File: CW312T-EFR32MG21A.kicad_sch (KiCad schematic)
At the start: 18 parts, among them J1 1x3 straight header pins, P1 PCIEx4 EDGE CONNECTOR, U1 EFR32MG21A020F1024IM32-BR

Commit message: first draft - ready for review
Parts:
- added PCB1: CE Symbol, Silkscrren_Symbols:CE-Logo_8.5x6mm_SilkScreen, symbol Silkscreen_Symbols:CE_Free
- added PCB2: Pb_Free Symbol, Silkscrren_Symbols:Pb_Free_8.0x8.0mm_SilkScreen, symbol Silkscreen_Symbols:Pb_Free
- added PCB3: UKCA symbol, Silkscrren_Symbols:UKCA-Logo_8x8mm_SilkScreen, symbol Silkscreen_Symbols:UKCA
- added PCB4: WEEE SYMBOL, Silkscrren_Symbols:WEEE-Logo_5.6x8mm_SilkScreen, symbol Silkscreen_Symbols:WEEE
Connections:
- net GND: now also U1.33 (VSS); no longer U1.0 (VSS)

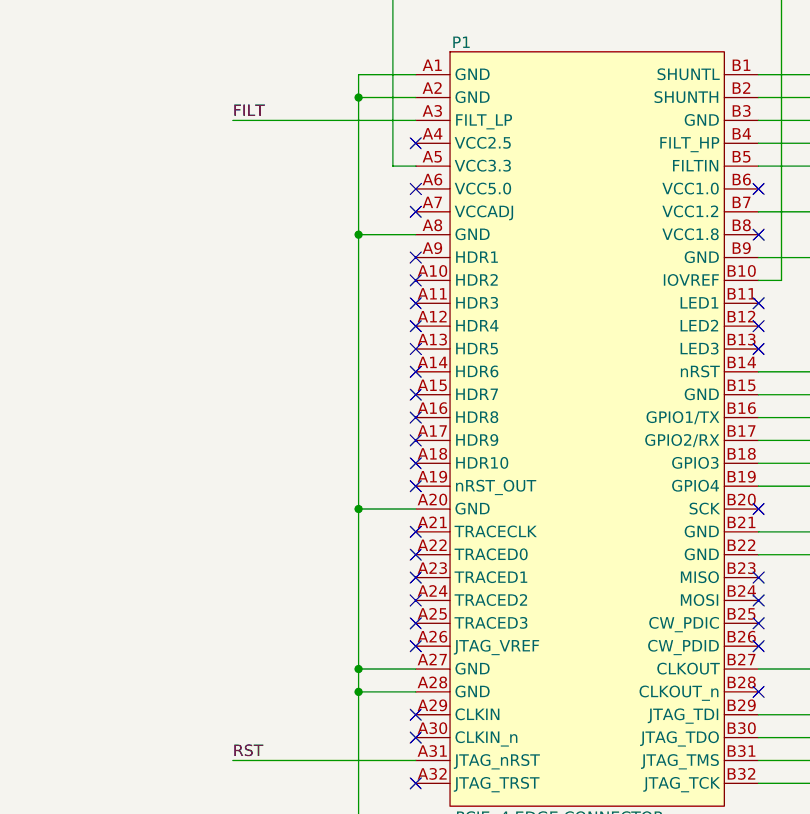
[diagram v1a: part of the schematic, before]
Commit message: updated schematic to fix power, updated pcb and production files - ready for review
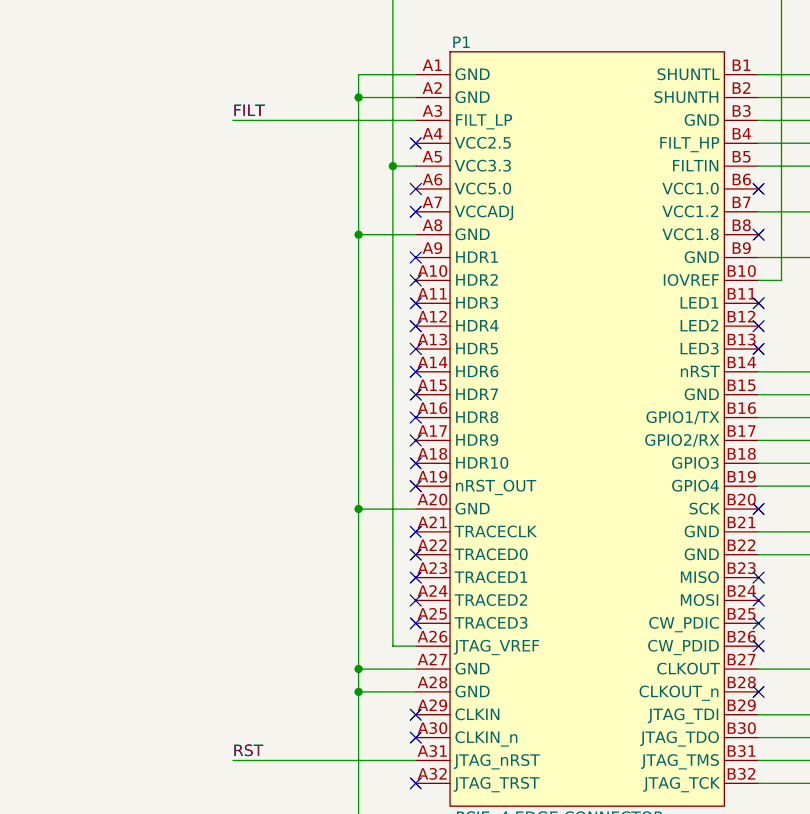
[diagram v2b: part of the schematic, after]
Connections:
- net +3V3: now also P1.A26 (JTAG_VREF)
- no-connect marks 47 -> 46
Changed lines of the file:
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@@
+	)
+	(junction
+		(at 39.37 62.23)
+		(diameter 0)
+		(color 0 0 0 0)
 	)
 	(junction
@@
 	)
 	(no_connect
-		(at 41.91 115.57)
-	)
-	(no_connect
 		(at 41.91 107.95)
 	)
@@
 	(wire
 		(pts
+			(xy 39.37 62.23) (xy 39.37 115.57)
+		)
+		(stroke
+			(width 0)
+			(type default)
+		)
+	)
+	(wire
+		(pts
 			(xy 35.56 120.65) (xy 41.91 120.65)
 		)
@@
 		)
 		(stroke
+			(width 0)
+			(type default)
+		)
+	)
+	(wire
+		(pts
+			(xy 41.91 115.57) (xy 39.37 115.57)
+		)
+		(stroke

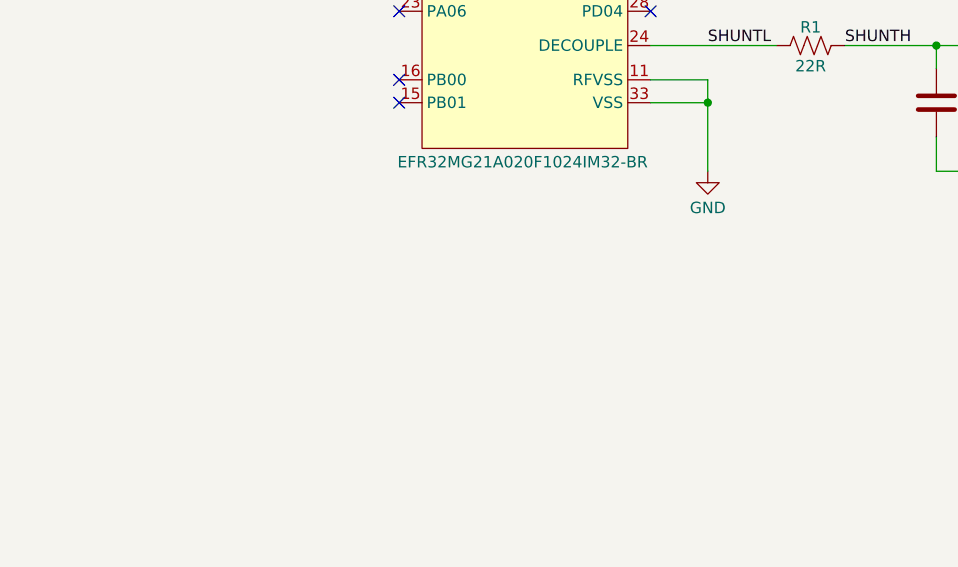
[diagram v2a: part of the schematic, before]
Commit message: added comment about footprint
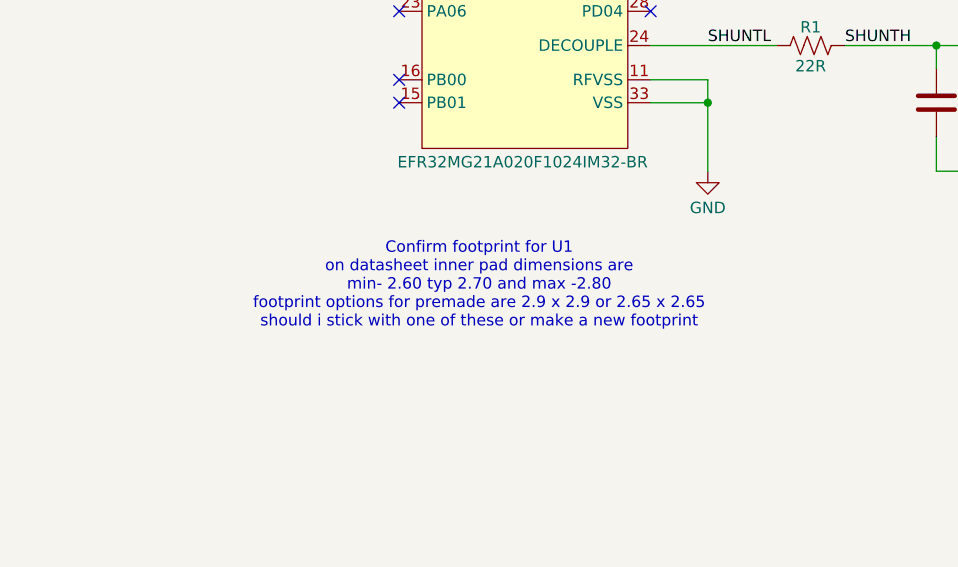
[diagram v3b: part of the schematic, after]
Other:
- note added: "Confirm footprint for U1 on datasheet inner pad dimensions are min- 2.60 typ 2.70 and max -2.80 footprint options for premade are 2.9 x 2.9 or 2.65 x 2.65 should i stick with one of these or make a new footprint"
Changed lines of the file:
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@@
+		)
+	)
+	(text "Confirm footprint for U1 \non datasheet inner pad dimensions are \nmin- 2.60 typ 2.70 and max -2.80 \nfootprint options for premade are 2.9 x 2.9 or 2.65 x 2.65\nshould i stick with one of these or make a new footprint\n"
+		(exclude_from_sim no)
+		(at 195.58 156.21 0)
+		(effects
+			(font
+				(size 1.27 1.27)
+			)
 		)
 	)

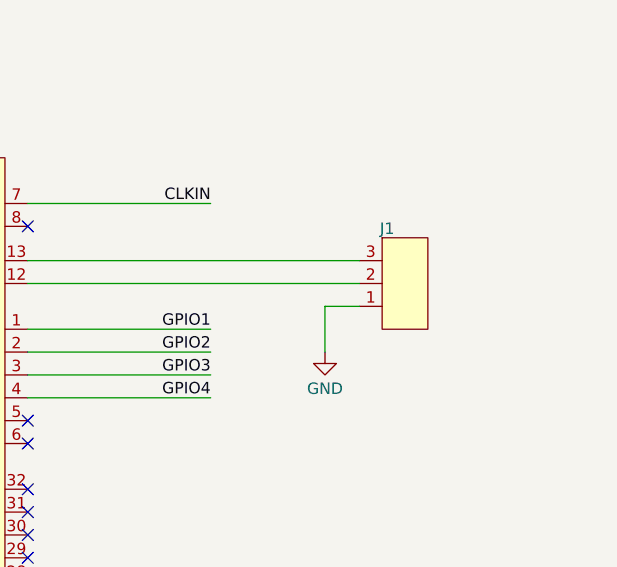
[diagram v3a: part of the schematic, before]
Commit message: updated 3 pin header to fix footprint
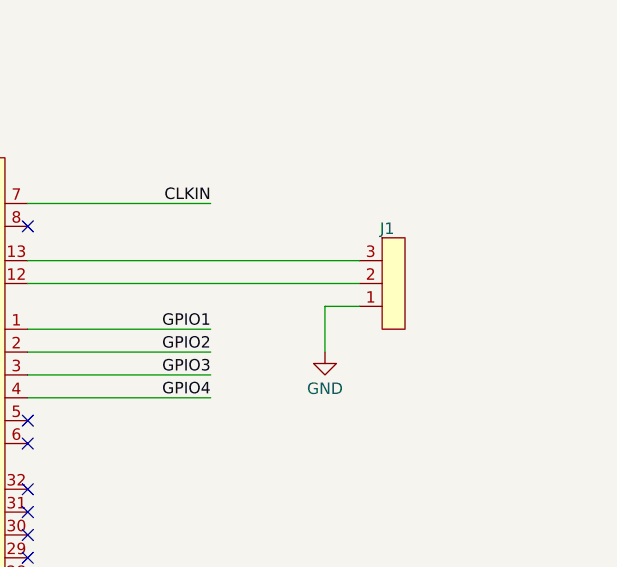
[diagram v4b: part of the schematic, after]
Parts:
- removed J1: 1x3 straight header pins, Connector_PinHeader_1.00mm:PinHeader_1x03_P1.00mm_Vertical, symbol tutorial_2_library:1x3 header 2.54mm
- added J1: 1x3 straight header pins, Connector_PinHeader_2.54mm:PinHeader_1x03_P2.54mm_Vertical, symbol tutorial_2_library:VERT_HDR_3_2.54mm
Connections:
- net GND: now also J1.1
- net at U1.12 (RF2G4_IO2): now also J1.2
- net at U1.13 (RF2G4_IO1): now also J1.3
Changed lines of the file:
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@@
-	)
-	(symbol
-		(lib_id "tutorial_2_library:1x3 header 2.54mm")
-		(at 254 90.17 0)
-		(unit 1)
-		(exclude_from_sim no)
-		(in_bom yes)
-		(on_board yes)
-		(dnp no)
-		(property "Reference" "J1"
-			(at 253.746 86.614 0)
-			(effects
-				(font
-					(size 1.27 1.27)
-				)
-				(justify left)
-			)
-		)
-		(property "Value" "1x3 straight header pins"
-			(at 265.43 161.29 0)
-			(effects
-				(font
-					(size 1.27 1.27)
-				)
-				(hide yes)
-			)
-		)
-		(property "Footprint" "Connector_PinHeader_1.00mm:PinHeader_1x03_P1.00mm_Vertical"
-			(at 254 157.48 0)
-			(effects
-				(font
-					(size 1.27 1.27)
-				)
-				(hide yes)
-			)
-		)
-		(property "Datasheet" "https://www.we-online.com/components/products/datasheet/61300311121.pdf"
-			(at 284.48 152.4 0)
-			(effects
-				(font
-					(size 1.27 1.27)
-				)
-				(hide yes)
-			)
-		)
-		(property "Description" "CONN HEADER VERT 3POS 2.54MM"
-			(at 274.32 149.86 0)
-			(effects
-				(font
-					(size 1.27 1.27)
-				)
-				(hide yes)
-			)
-		)
-		(property "Display Value" "Header"
-			(at 256.54 99.06 0)
-			(effects
-				(font
-					(size 1.27 1.27)
-				)
-				(hide yes)
-			)
-		)
-		(property "Manufacturer" "Würth Elektronik"
-			(at 245.11 161.29 0)
-			(effects
-				(font
-					(size 1.27 1.27)
-				)
-				(hide yes)
-			)
-		)
-		(property "Manufacturer Part Number" "61300311121"
-			(at 243.84 154.94 0)
-			(effects
-				(font
-					(size 1.27 1.27)
-				)
-				(hide yes)
-			)
-		)
-		(property "Supplier 1" "DigiKey"
-			(at 238.76 163.83 0)
-			(effects
-				(font
-					(size 1.27 1.27)
-				)
-				(hide yes)
-			)
-		)
-		(property "Supplier 1 Part Number" "732-5316-ND"
-			(at 266.7 163.83 0)
-			(effects
-				(font
-					(size 1.27 1.27)
-				)
-				(hide yes)
-			)
-		)
-		(property "Supplier 2" ""
-			(at 251.46 90.17 0)
-			(effects
-				(font
-					(size 1.27 1.27)
-				)
-				(hide yes)
-			)
-		)
-		(property "Supplier 2 Part Number" ""
-			(at 251.46 90.17 0)
-			(effects
-				(font
-					(size 1.27 1.27)
-				)
-				(hide yes)
-			)
-		)
-		(pin "3"
-		)
-		(pin "1"
-		)
-		(pin "2"
-		)
-		(instances
-			(project ""
-				(path "/701bca9e-bb11-47dc-a816-b9cd0999f76c"
-					(reference "J1")
-					(unit 1)
-				)
-			)
-		)
 	)
 	(symbol
@@
 					(unit 1)
 				)
+			)
+		)
+	)
+	(symbol
+		(lib_id "tutorial_2_library:VERT_HDR_3_2.54mm")
+		(at 254 90.17 0)
+		(unit 1)
+		(exclude_from_sim no)
+		(in_bom yes)
+		(on_board yes)
+		(dnp no)
+		(property "Reference" "J1"
+			(at 253.746 86.614 0)
+			(effects
+				(font
+					(size 1.27 1.27)
+				)
+				(justify left)
+			)
+		)
+		(property "Value" "1x3 straight header pins"
+			(at 265.43 161.29 0)
+			(effects
+				(font
+					(size 1.27 1.27)
+				)
+				(hide yes)
+			)
+		)
+		(property "Footprint" "Connector_PinHeader_2.54mm:PinHeader_1x03_P2.54mm_Vertical"
+			(at 254 157.48 0)
+			(effects
+				(font
+					(size 1.27 1.27)
+				)
+				(hide yes)
+			)
+		)
+		(property "Datasheet" "https://www.we-online.com/components/products/datasheet/61300311121.pdf"
+			(at 284.48 152.4 0)
+			(effects
+				(font
+					(size 1.27 1.27)
+				)
+				(hide yes)
+			)
+		)
+		(property "Description" "CONN HEADER VERT 3POS 2.54MM"
+			(at 274.32 149.86 0)
+			(effects
+				(font
+					(size 1.27 1.27)
+				)
+				(hide yes)
+			)
+		)
+		(property "Display Value" "Header"
+			(at 256.54 99.06 0)
+			(effects
+				(font
+					(size 1.27 1.27)
+				)
+				(hide yes)
+			)
+		)
+		(property "Manufacturer" "Würth Elektronik"
+			(at 245.11 161.29 0)
+			(effects
+				(font
+					(size 1.27 1.27)
+				)
+				(hide yes)
+			)
+		)
+		(property "Manufacturer Part Number" "61300311121"
+			(at 243.84 154.94 0)
+			(effects
+				(font
+					(size 1.27 1.27)
+				)
+				(hide yes)
+			)
+		)
+		(property "Supplier 1" "DigiKey"
+			(at 238.76 163.83 0)
+			(effects
+				(font
+					(size 1.27 1.27)
+				)
+				(hide yes)
+			)
+		)
+		(property "Supplier 1 Part Number" "732-5316-ND"
+			(at 266.7 163.83 0)
+			(effects
+				(font
+					(size 1.27 1.27)
+				)
+				(hide yes)
+			)
+		)
+		(property "Supplier 2" ""
+			(at 251.46 90.17 0)
+			(effects
+				(font
+					(size 1.27 1.27)
+				)
+				(hide yes)
+			)
+		)
+		(property "Supplier 2 Part Number" ""
+			(at 251.46 90.17 0)
+			(effects
+				(font
+					(size 1.27 1.27)
+				)
+				(hide yes)
+			)
+		)
+		(pin "1"
+		)
+		(pin "3"
+		)
+		(pin "2"
+		)
+		(instances
+			(project ""
+				(path "/701bca9e-bb11-47dc-a816-b9cd0999f76c"
+					(reference "J1")
+					(unit 1)
+				)

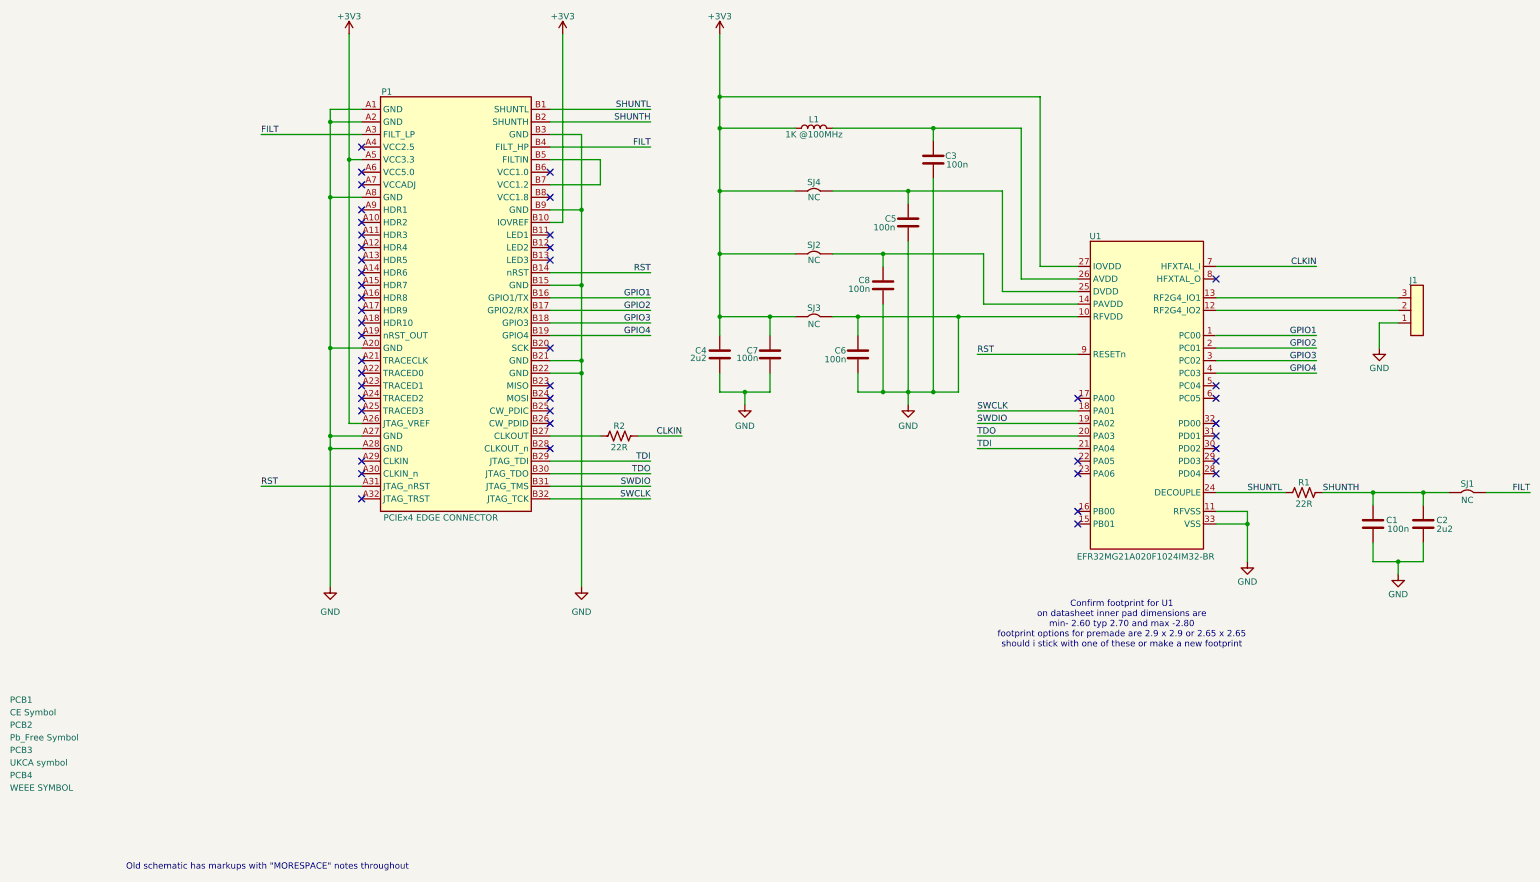
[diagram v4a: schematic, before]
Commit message: updated schematic and pcb after library reorganization
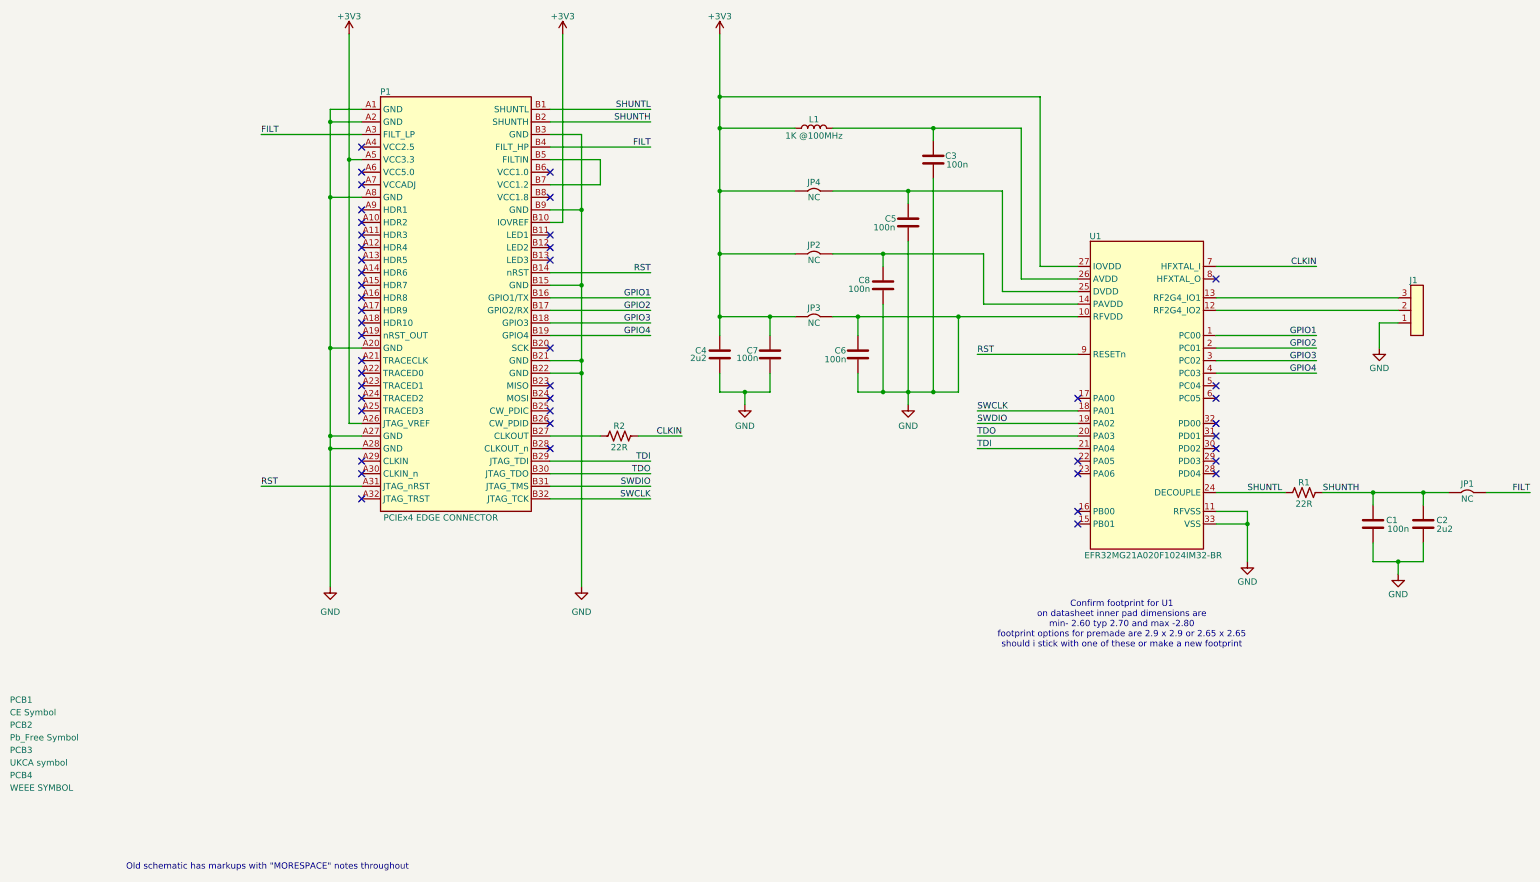
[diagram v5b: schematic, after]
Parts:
- removed J1: 1x3 straight header pins, Connector_PinHeader_2.54mm:PinHeader_1x03_P2.54mm_Vertical, symbol tutorial_2_library:VERT_HDR_3_2.54mm
- removed L1: IND_1K_0603, Inductor_SMD:L_0603_1608Metric, symbol tutorial_2_library:IND_1K_100MHz_0603
- removed P1: PCIEx4 EDGE CONNECTOR, tutorial_2_library:CW312_Template, symbol tutorial_2_library:CW312T-Template
- removed SJ1, SJ2, SJ3, SJ4: ~, Jumper:SolderJumper-2_P1.3mm_Bridged2Bar_Pad1.0x1.5mm, symbol tutorial_2_library:Solder_Jumper_2_NC
- removed U1: EFR32MG21A020F1024IM32-BR, Package_DFN_QFN:QFN-32-1EP_4x4mm_P0.4mm_EP2.9x2.9mm, symbol tutorial_2_library:EFR32MG21A020F1024IM32-BR
- added J1: 1x3 straight header pins, Connector_PinHeader_2.54mm:PinHeader_1x03_P2.54mm_Vertical, symbol NAE_Connectors:VERT_HDR_3_2.54mm
- added JP1, JP2, JP3, JP4: ~, Jumper:SolderJumper-2_P1.3mm_Bridged2Bar_Pad1.0x1.5mm, symbol NAE_Connectors:Solder_Jumper_2_NC
- added L1: IND_1K_0603, Inductor_SMD:L_0603_1608Metric, symbol NAE_Inductors:IND_1K_100MHz_0603
- added P1: PCIEx4 EDGE CONNECTOR, tutorial_2_library:CW312_Template, symbol NAE_Connectors:CW312T-Template
- added U1: EFR32MG21A020F1024IM32-BR, Package_DFN_QFN:QFN-32-1EP_4x4mm_P0.4mm_EP2.9x2.9mm, symbol NAE_Integrated_Circuits:EFR32MG21A020F1024IM32-BR
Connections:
- net +3V3: now also JP2.2, JP3.2, JP4.2, L1.1, P1.A26 (JTAG_VREF), P1.A5 (VCC3.3), P1.B10 (IOVREF), U1.27 (IOVDD)
- net CLKIN: now also U1.7 (HFXTAL_I)
- net FILT: now also JP1.1, P1.A3 (FILT_LP), P1.B4 (FILT_HP)
- net GND: now also J1.1, JP3.1, P1.A1 (GND), P1.A2 (GND), P1.A20 (GND), P1.A27 (GND), P1.A28 (GND), P1.A8 (GND), P1.B15 (GND), P1.B21 (GND), P1.B22 (GND), P1.B3 (GND), P1.B9 (GND), U1.10 (RFVDD), U1.11 (RFVSS), U1.33 (VSS)
- net GPIO1: now also P1.B16 (GPIO1/TX), U1.1 (PC00)
- net GPIO2: now also P1.B17 (GPIO2/RX), U1.2 (PC01)
- net GPIO3: now also P1.B18 (GPIO3), U1.3 (PC02)
- net GPIO4: now also P1.B19 (GPIO4), U1.4 (PC03)
- net RST: now also P1.A31 (JTAG_nRST), P1.B14 (nRST), U1.9 (RESETn)
- net SHUNTH: now also JP1.2, P1.B2 (SHUNTH)
- net SHUNTL: now also P1.B1 (SHUNTL), U1.24 (DECOUPLE)
- net SWCLK: now also P1.B32 (JTAG_TCK), U1.18 (PA01)
- net SWDIO: now also P1.B31 (JTAG_TMS), U1.19 (PA02)
- net TDI: now also P1.B29 (JTAG_TDI), U1.21 (PA04)
- net TDO: now also P1.B30 (JTAG_TDO), U1.20 (PA03)
- net at C8.2: now also JP2.1, U1.14 (PAVDD)
- net at C5.2: now also JP4.1, U1.25 (DVDD)
- net at C3.2: now also L1.2, U1.26 (AVDD)
- net at R2.1: now also P1.B27 (CLKOUT)
- new net: P1.B5 (FILTIN), P1.B7 (VCC1.2)
- new net: J1.2, U1.12 (RF2G4_IO2)
- new net: J1.3, U1.13 (RF2G4_IO1)
